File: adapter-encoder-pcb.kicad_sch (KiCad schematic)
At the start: 23 parts, among them IC2 THVD2410VDRCR, M1 THRU_HOLE_PAD, M2 THRU_HOLE_PAD, U1 TLE5009E1000FUMA1, U2 STM32L011F4Ux, U3 DF52-4S-0.8H(21), U4 SPX3819M5-L-3-3

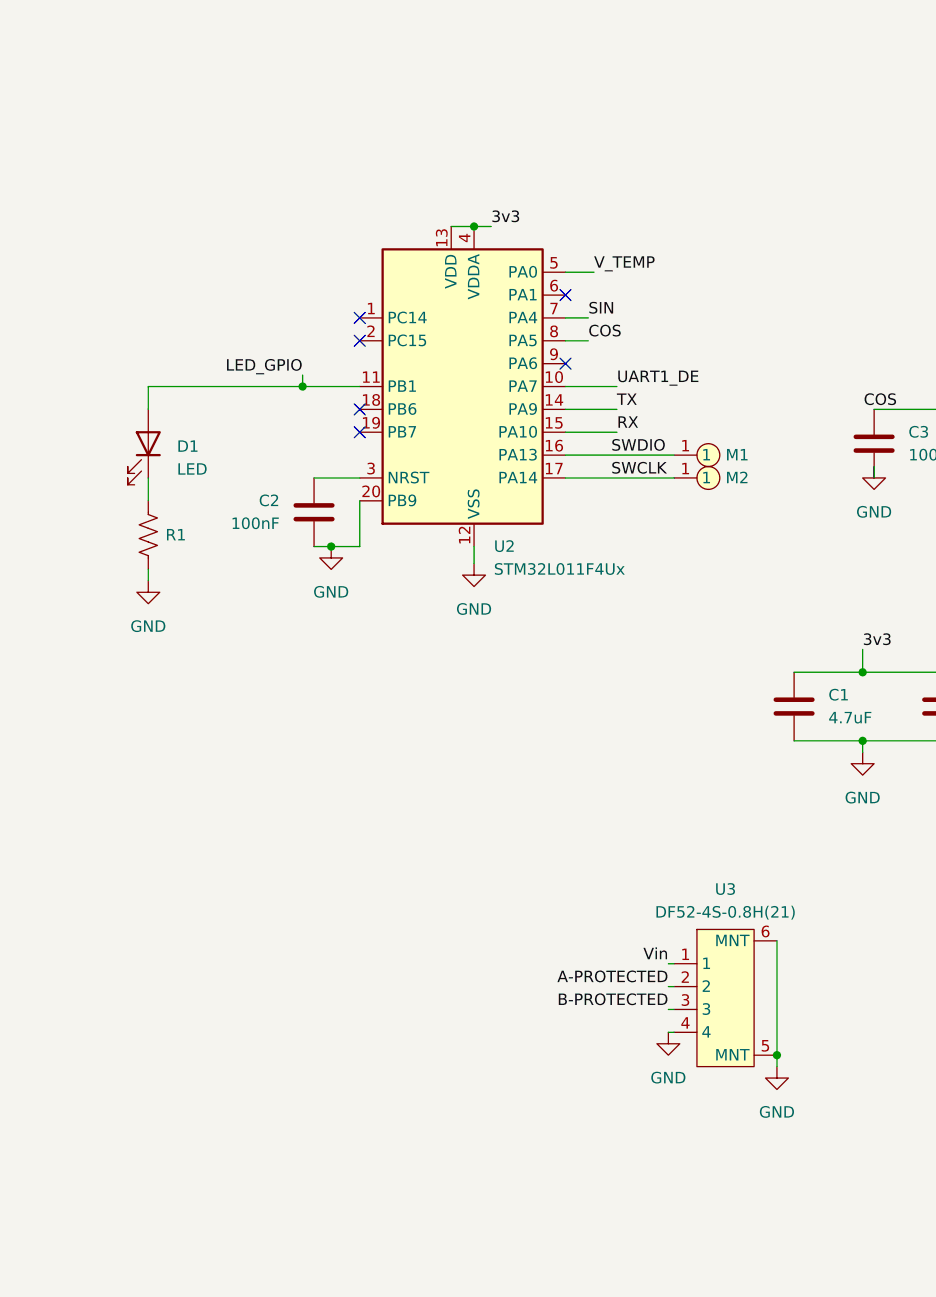
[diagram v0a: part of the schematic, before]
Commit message: new STM32, not enough RAM on the shitty L0. will probably need a little more OD but thats ok
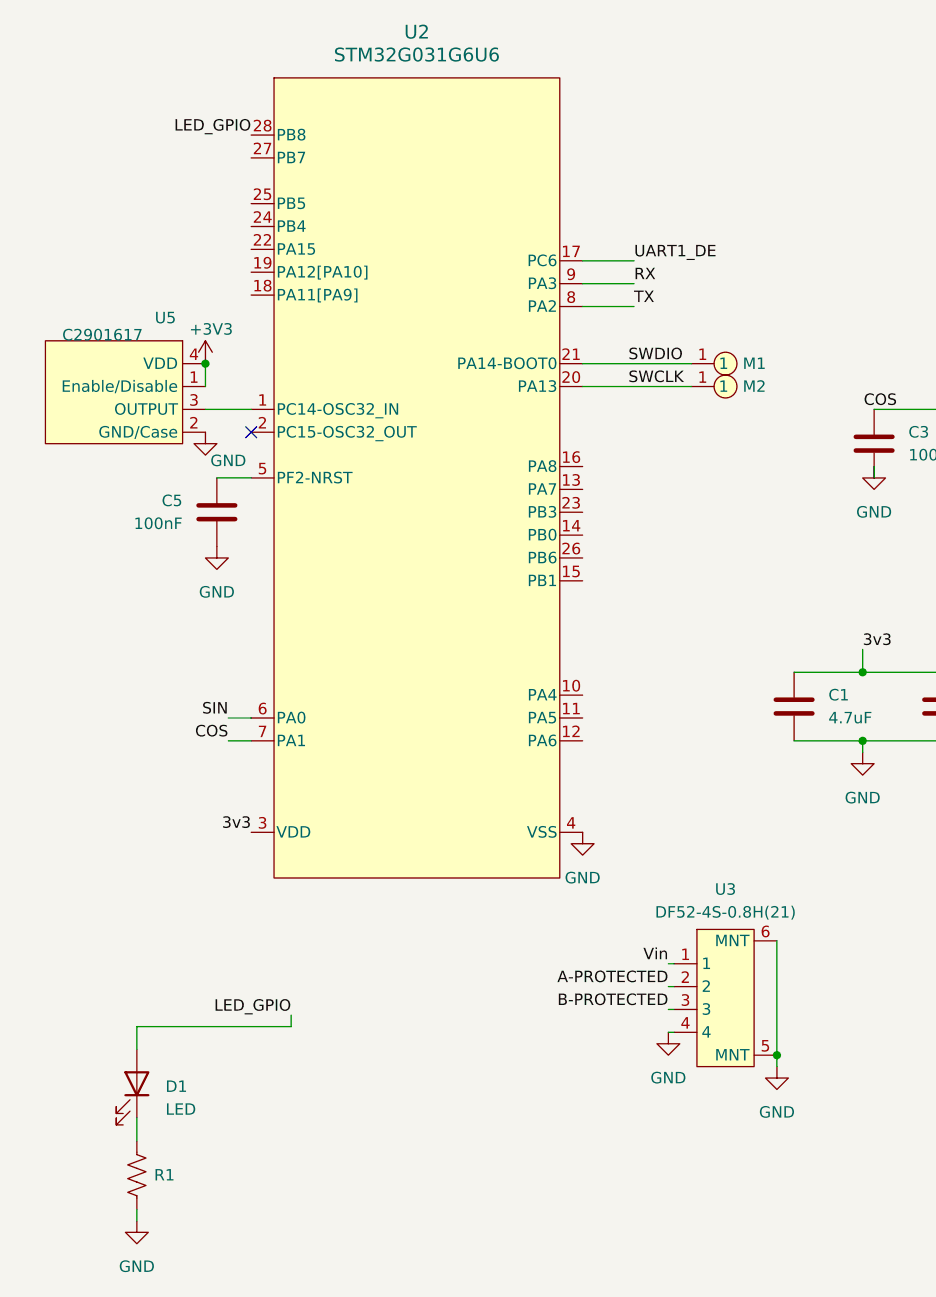
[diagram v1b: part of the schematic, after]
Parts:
- removed C2: 100nF, adapter-encoder:C_0402_1005Metric, symbol adapter-encoder:Capacitor
- removed U2: STM32L011F4Ux, adapter-encoder:ST_UFQFPN-20_3x3mm_P0.5mm, symbol adapter-encoder:STM32L011F4Ux
- added C5: 100nF, adapter-encoder:C_0402_1005Metric, symbol adapter-encoder:Capacitor
- added U2: STM32G031G6U6, foc-pcb-library:UFQFPN28, symbol adapter-encoder:STM32G031G6U6
- added U5: C2901617, foc-pcb-library:ECS-1633-480-BN-TR, symbol foc-pcb:OSCILLATOR-4PIN
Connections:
- net +3V3: now also U5.1 (Enable/Disable), U5.4 (VDD)
- net 3v3: now also U2.3 (VDD)
- net COS: now also U2.7 (PA1)
- net GND: now also C5.2, U2.4 (VSS), U5.2 (GND/Case)
- net LED_GPIO: now also U2.28 (PB8)
- net RX: now also U2.9 (PA3)
- net SIN: now also U2.6 (PA0)
- net SWCLK: now also U2.20 (PA13)
- net SWDIO: now also U2.21 (PA14-BOOT0)
- net TX: now also U2.8 (PA2)
- net UART1_DE: now also U2.17 (PC6)
- new net: C5.1, U2.5 (PF2-NRST)
- new net: U2.1 (PC14-OSC32_IN), U5.3 (OUTPUT)
- no-connect marks 10 -> 5
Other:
- moved on the sheet: D1, R1

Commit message: mostly routed updated board
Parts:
- added C12, C15, C17: 4.7uF, adapter-encoder:C_0603_1608Metric, symbol adapter-encoder:Capacitor
- added C13, C14, C16, C18: 100nF, adapter-encoder:C_0402_1005Metric, symbol adapter-encoder:Capacitor
- added U6: DF52-4S-0.8H(21), adapter-encoder:DF52-4S-0.8H(21), symbol adapter-encoder:DF52-4S-0.8H(21)
- added U7: SPX3819M5-L-3-3, adapter-encoder:SOT-23-5, symbol adapter-encoder:SPX3819M5-L-3-3
- D1, R1: now in the parts list
- U2: footprint foc-pcb-library:UFQFPN28 -> adapter-encoder:UFQFPN28
- U5: footprint foc-pcb-library:ECS-1633-480-BN-TR -> adapter-encoder:ECS-1633-480-BN-TR; symbol foc-pcb:OSCILLATOR-4PIN -> adapter-encoder:OSCILLATOR-4PIN
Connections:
- net 3v3 is gone; now on net +3V3: C1.1, C2.1, U1.6 (Vdd), U2.3 (VDD), U4.5 (VOUT)
- net +3V3: now also C12.1, C13.1
- net +5V0: now also C16.1, C17.1, U7.5 (VOUT)
- net A-PROTECTED: now also U6.2
- net B-PROTECTED: now also U6.3
- net GND: now also C12.2, C13.2, C14.2, C15.2, C16.2, C17.2, C18.2, U6.4, U6.5 (MNT), U6.6 (MNT), U7.2 (GND)
- net LED_GPIO: now also U2.27 (PB7); no longer U2.28 (PB8)
- net Vin: now also C14.1, C15.1, C18.1, U6.1, U7.1 (VIN), U7.3 (EN)
- no-connect marks 5 -> 6
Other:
- moved on the sheet: C2

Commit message: length matching rs485
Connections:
- net A-PROTECTED renamed RS485+
- net B-PROTECTED renamed RS485-
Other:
- moved on the sheet: C36, C37, IC2, R16, R8, R9, U3
